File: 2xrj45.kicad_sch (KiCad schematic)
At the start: 33 parts, among them J1 Bus_RJ45_JTH-0024NL, J10 MP_Terminal_M3_SMD_7466303R, J2 Bus_RJ45_JTH-0024NL, J9 MP_Terminal_M3_SMD_7466303R

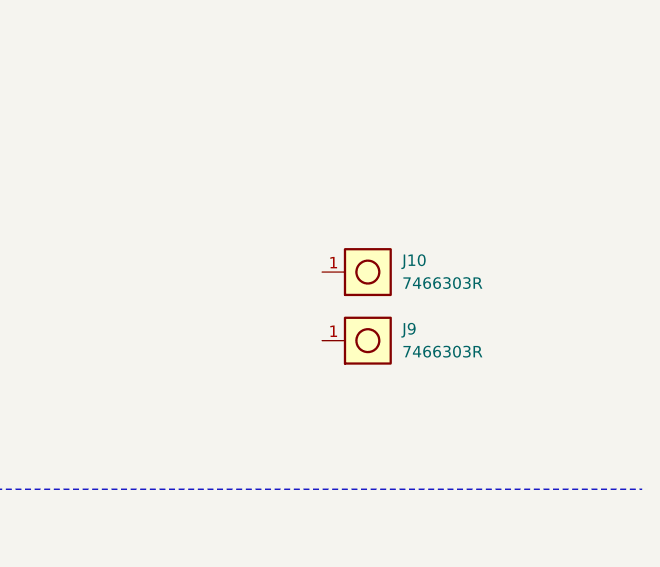
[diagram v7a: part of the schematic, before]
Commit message: [#80813] Change PCB mounts, replace NCSI connector with testpoints
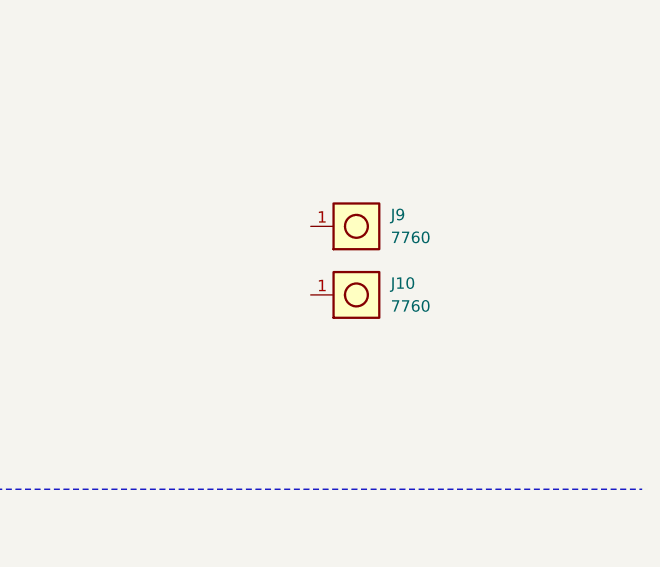
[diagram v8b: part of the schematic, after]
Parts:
- removed J10, J9: MP_Terminal_M3_SMD_7466303R, antmicro-footprints:MP_Terminal_M3_SMD_7466303R, symbol antmicroMechanicalParts:MP_Terminal_M3_SMD_7466303R
- added J10, J9: MP_Terminal_M3_THT_7760, antmicro-footprints:MP_Terminal_M3_THT_7760, symbol antmicroMechanicalParts:MP_Terminal_M3_THT_7760
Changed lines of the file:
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@@
-	)
-	(symbol
-		(lib_id "antmicroMechanicalParts:MP_Terminal_M3_SMD_7466303R")
-		(at 372.11 127 0)
-		(unit 1)
-		(exclude_from_sim no)
-		(in_bom yes)
-		(on_board yes)
-		(dnp no)
-		(fields_autoplaced yes)
-		(property "Reference" "J9"
-			(at 381 125.73 0)
-			(effects
-				(font
-					(size 1.27 1.27)
-					(thickness 0.15)
-				)
-				(justify left)
-			)
-		)
-		(property "Value" "MP_Terminal_M3_SMD_7466303R"
-			(at 394.97 134.62 0)
-			(effects
-				(font
-					(size 1.27 1.27)
-					(thickness 0.15)
-				)
-				(justify left bottom)
-				(hide yes)
-			)
-		)
-		(property "Footprint" "antmicro-footprints:MP_Terminal_M3_SMD_7466303R"
-			(at 394.97 137.16 0)
-			(effects
-				(font
-					(size 1.27 1.27)
-					(thickness 0.15)
-				)
-				(justify left bottom)
-				(hide yes)
-			)
-		)
-		(property "Datasheet" "https://www.mouser.com/datasheet/2/445/7466303-2890962.pdf"
-			(at 394.97 139.7 0)
-			(effects
-				(font
-					(size 1.27 1.27)
-					(thickness 0.15)
-				)
-				(justify left bottom)
-				(hide yes)
-			)
-		)
-		(property "Description" "PCB Terminal, 90° SMT Block, Brass, Tin, REDCUBE WP-SMRA"
-			(at 372.11 127 0)
-			(effects
-				(font
-					(size 1.27 1.27)
-				)
-				(hide yes)
-			)
-		)
-		(property "MPN" "7466303R"
-			(at 381 128.27 0)
-			(effects
-				(font
-					(size 1.27 1.27)
-					(thickness 0.15)
-				)
-				(justify left)
-			)
-		)
-		(property "Manufacturer" "Würth Elektronik"
-			(at 394.97 142.24 0)
-			(effects
-				(font
-					(size 1.27 1.27)
-					(thickness 0.15)
-				)
-				(justify left bottom)
-				(hide yes)
-			)
-		)
-		(property "Author" "Antmicro"
-			(at 394.97 144.78 0)
-			(effects
-				(font
-					(size 1.27 1.27)
-					(thickness 0.15)
-				)
-				(justify left bottom)
-				(hide yes)
-			)
-		)
-		(property "License" "Apache-2.0"
-			(at 394.97 147.32 0)
-			(effects
-				(font
-					(size 1.27 1.27)
-					(thickness 0.15)
-				)
-				(justify left bottom)
-				(hide yes)
-			)
-		)
-		(pin "1"
-		)
-		(instances
-			(project "10-gbe-expansion"
-				(path "/04bda987-e5eb-48b4-9e90-d8211dc11b39/b3dd2e9f-aefc-4b19-a6a4-069fdee319cd"
-					(reference "J9")
-					(unit 1)
-				)
-			)
-		)
 	)
 	(symbol
@@
 	)
 	(symbol
+		(lib_id "antmicroMechanicalParts:MP_Terminal_M3_THT_7760")
+		(at 370.84 121.92 0)
+		(unit 1)
+		(exclude_from_sim no)
+		(in_bom yes)
+		(on_board yes)
+		(dnp no)
+		(fields_autoplaced yes)
+		(property "Reference" "J10"
+			(at 379.73 120.65 0)
+			(effects
+				(font
+					(size 1.27 1.27)
+					(thickness 0.15)
+				)
+				(justify left)
+			)
+		)
+		(property "Value" "MP_Terminal_M3_THT_7760"
+			(at 393.7 129.54 0)
+			(effects
+				(font
+					(size 1.27 1.27)
+					(thickness 0.15)
+				)
+				(justify left bottom)
+				(hide yes)
+			)
+		)
+		(property "Footprint" "antmicro-footprints:MP_Terminal_M3_THT_7760"
+			(at 393.7 132.08 0)
+			(effects
+				(font
+					(size 1.27 1.27)
+					(thickness 0.15)
+				)
+				(justify left bottom)
+				(hide yes)
+			)
+		)
+		(property "Datasheet" "https://www.mouser.pl/datasheet/2/215/7760-741244.pdf"
+			(at 393.7 134.62 0)
+			(effects
+				(font
+					(size 1.27 1.27)
+					(thickness 0.15)
+				)
+				(justify left bottom)
+				(hide yes)
+			)
+		)
+		(property "Description" "PCB Terminal, 90° THT, Brass, Tin"
+			(at 393.7 137.16 0)
+			(effects
+				(font
+					(size 1.27 1.27)
+					(thickness 0.15)
+				)
+				(justify left bottom)
+				(hide yes)
+			)
+		)
+		(property "MPN" "7760"
+			(at 379.73 123.19 0)
+			(effects
+				(font
+					(size 1.27 1.27)
+					(thickness 0.15)
+				)
+				(justify left)
+			)
+		)
+		(property "Manufacturer" "Keystone Electronics"
+			(at 393.7 139.7 0)
+			(effects
+				(font
+					(size 1.27 1.27)
+					(thickness 0.15)
+				)
+				(justify left bottom)
+				(hide yes)
+			)
+		)
+		(property "Author" "Antmicro"
+			(at 393.7 142.24 0)
+			(effects
+				(font
+					(size 1.27 1.27)
+					(thickness 0.15)
+				)
+				(justify left bottom)
+				(hide yes)
+			)
+		)
+		(property "License" "Apache-2.0"
+			(at 393.7 144.78 0)
+			(effects
+				(font
+					(size 1.27 1.27)
+					(thickness 0.15)
+				)
+				(justify left bottom)
+				(hide yes)
+			)
+		)
+		(pin "1"
+		)
+		(instances
+			(project "10-gbe-expansion"
+				(path "/04bda987-e5eb-48b4-9e90-d8211dc11b39/b3dd2e9f-aefc-4b19-a6a4-069fdee319cd"
+					(reference "J10")
+					(unit 1)
+				)
+			)
+		)
+	)
+	(symbol
 		(lib_id "antmicropower:GND")
 		(at 228.6 107.95 0)
@@
 				(path "/04bda987-e5eb-48b4-9e90-d8211dc11b39/b3dd2e9f-aefc-4b19-a6a4-069fdee319cd"
 					(reference "C2")
+					(unit 1)
+				)
+			)
+		)
+	)
+	(symbol
+		(lib_id "antmicroMechanicalParts:MP_Terminal_M3_THT_7760")
+		(at 370.84 114.3 0)
+		(unit 1)
+		(exclude_from_sim no)
+		(in_bom yes)
+		(on_board yes)
+		(dnp no)
+		(fields_autoplaced yes)
+		(property "Reference" "J9"
+			(at 379.73 113.03 0)
+			(effects
+				(font
+					(size 1.27 1.27)
+					(thickness 0.15)
+				)
+				(justify left)
+			)
+		)
+		(property "Value" "MP_Terminal_M3_THT_7760"
+			(at 393.7 121.92 0)
+			(effects
+				(font
+					(size 1.27 1.27)
+					(thickness 0.15)
+				)
+				(justify left bottom)
+				(hide yes)
+			)
+		)
+		(property "Footprint" "antmicro-footprints:MP_Terminal_M3_THT_7760"
+			(at 393.7 124.46 0)
+			(effects
+				(font
+					(size 1.27 1.27)
+					(thickness 0.15)
+				)
+				(justify left bottom)
+				(hide yes)
+			)
+		)
+		(property "Datasheet" "https://www.mouser.pl/datasheet/2/215/7760-741244.pdf"
+			(at 393.7 127 0)
+			(effects
+				(font
+					(size 1.27 1.27)
+					(thickness 0.15)
+				)
+				(justify left bottom)
+				(hide yes)
+			)
+		)
+		(property "Description" "PCB Terminal, 90° THT, Brass, Tin"
+			(at 393.7 129.54 0)
+			(effects
+				(font
+					(size 1.27 1.27)
+					(thickness 0.15)
+				)
+				(justify left bottom)
+				(hide yes)
+			)
+		)
+		(property "MPN" "7760"
+			(at 379.73 115.57 0)
+			(effects
+				(font
+					(size 1.27 1.27)
+					(thickness 0.15)
+				)
+				(justify left)
+			)
+		)
+		(property "Manufacturer" "Keystone Electronics"
+			(at 393.7 132.08 0)
+			(effects
+				(font
+					(size 1.27 1.27)
+					(thickness 0.15)
+				)
+				(justify left bottom)
+				(hide yes)
+			)
+		)
+		(property "Author" "Antmicro"
+			(at 393.7 134.62 0)
+			(effects
+				(font
+					(size 1.27 1.27)
+					(thickness 0.15)
+				)
+				(justify left bottom)
+				(hide yes)
+			)
+		)
+		(property "License" "Apache-2.0"
+			(at 393.7 137.16 0)
+			(effects
+				(font
+					(size 1.27 1.27)
+					(thickness 0.15)
+				)
+				(justify left bottom)
+				(hide yes)
+			)
+		)
+		(pin "1"
+		)
+		(instances
+			(project "10-gbe-expansion"
+				(path "/04bda987-e5eb-48b4-9e90-d8211dc11b39/b3dd2e9f-aefc-4b19-a6a4-069fdee319cd"
+					(reference "J9")
 					(unit 1)
 				)
@@
 					(unit 1)
 				)
-			)
-		)
-	)
-	(symbol
-		(lib_id "antmicroMechanicalParts:MP_Terminal_M3_SMD_7466303R")
-		(at 372.11 119.38 0)
-		(unit 1)
-		(exclude_from_sim no)
-		(in_bom yes)
-		(on_board yes)
-		(dnp no)
-		(fields_autoplaced yes)
-		(property "Reference" "J10"
-			(at 381 118.11 0)
-			(effects
-				(font
-					(size 1.27 1.27)
-					(thickness 0.15)
-				)
-				(justify left)
-			)
-		)
-		(property "Value" "MP_Terminal_M3_SMD_7466303R"
-			(at 394.97 127 0)
-			(effects
-				(font
-					(size 1.27 1.27)
-					(thickness 0.15)
-				)
-				(justify left bottom)
-				(hide yes)
-			)
-		)
-		(property "Footprint" "antmicro-footprints:MP_Terminal_M3_SMD_7466303R"
-			(at 394.97 129.54 0)
-			(effects
-				(font
-					(size 1.27 1.27)
-					(thickness 0.15)
-				)
-				(justify left bottom)
-				(hide yes)
-			)
-		)
-		(property "Datasheet" "https://www.mouser.com/datasheet/2/445/7466303-2890962.pdf"
-			(at 394.97 132.08 0)
-			(effects
-				(font
-					(size 1.27 1.27)
-					(thickness 0.15)
-				)
-				(justify left bottom)
-				(hide yes)
-			)
-		)
-		(property "Description" "PCB Terminal, 90° SMT Block, Brass, Tin, REDCUBE WP-SMRA"
-			(at 372.11 119.38 0)
-			(effects
-				(font
-					(size 1.27 1.27)
-				)
-				(hide yes)
-			)
-		)
-		(property "MPN" "7466303R"
-			(at 381 120.65 0)
-			(effects
-				(font
-					(size 1.27 1.27)
-					(thickness 0.15)
-				)
-				(justify left)
-			)
-		)
-		(property "Manufacturer" "Würth Elektronik"
-			(at 394.97 134.62 0)
-			(effects
-				(font
-					(size 1.27 1.27)
-					(thickness 0.15)
-				)
-				(justify left bottom)
-				(hide yes)
-			)
-		)
-		(property "Author" "Antmicro"
-			(at 394.97 137.16 0)
-			(effects
-				(font
-					(size 1.27 1.27)
-					(thickness 0.15)
-				)
-				(justify left bottom)
-				(hide yes)
-			)
-		)
-		(property "License" "Apache-2.0"
-			(at 394.97 139.7 0)
-			(effects
-				(font
-					(size 1.27 1.27)
-					(thickness 0.15)
-				)
-				(justify left bottom)
-				(hide yes)
-			)
-		)
-		(pin "1"
-		)
-		(instances
-			(project "10-gbe-expansion"
-				(path "/04bda987-e5eb-48b4-9e90-d8211dc11b39/b3dd2e9f-aefc-4b19-a6a4-069fdee319cd"
-					(reference "J10")
-					(unit 1)
-				)
